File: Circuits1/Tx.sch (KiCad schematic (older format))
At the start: 28 parts, among them CON1 USB-MINI-B, SW1 SW_PUSH, U1 ATMEGA32U4, U2 LD1117, X1 QUARTZ

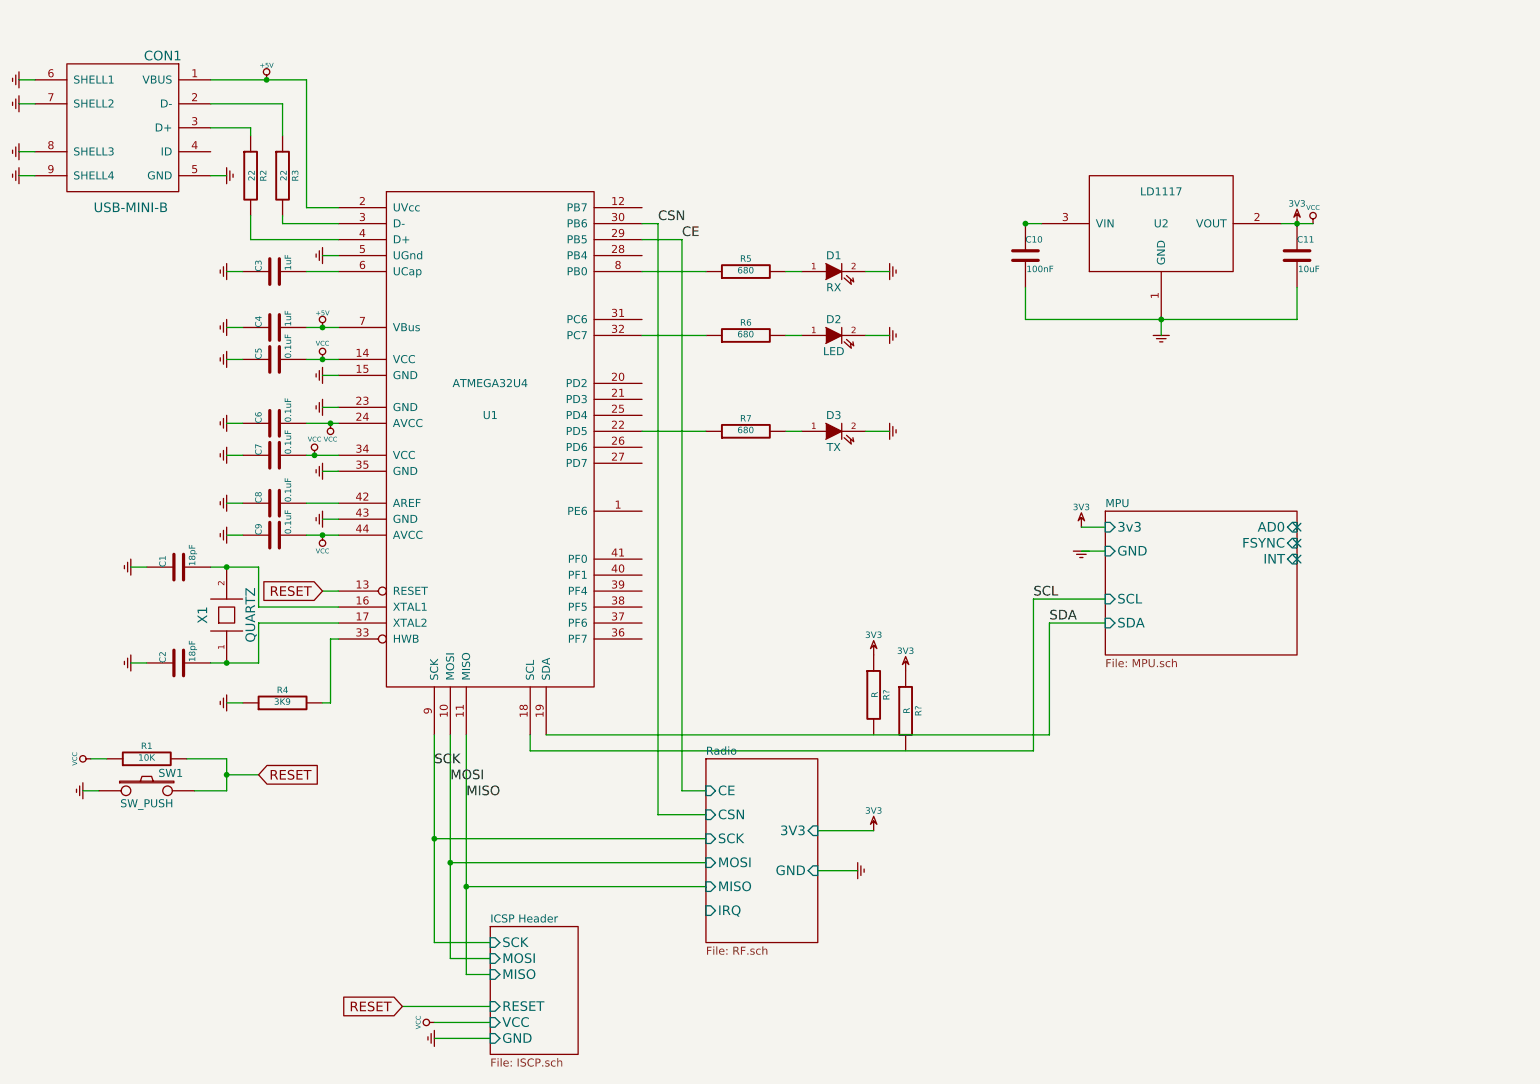
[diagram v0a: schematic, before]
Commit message: Tx Ground Planes
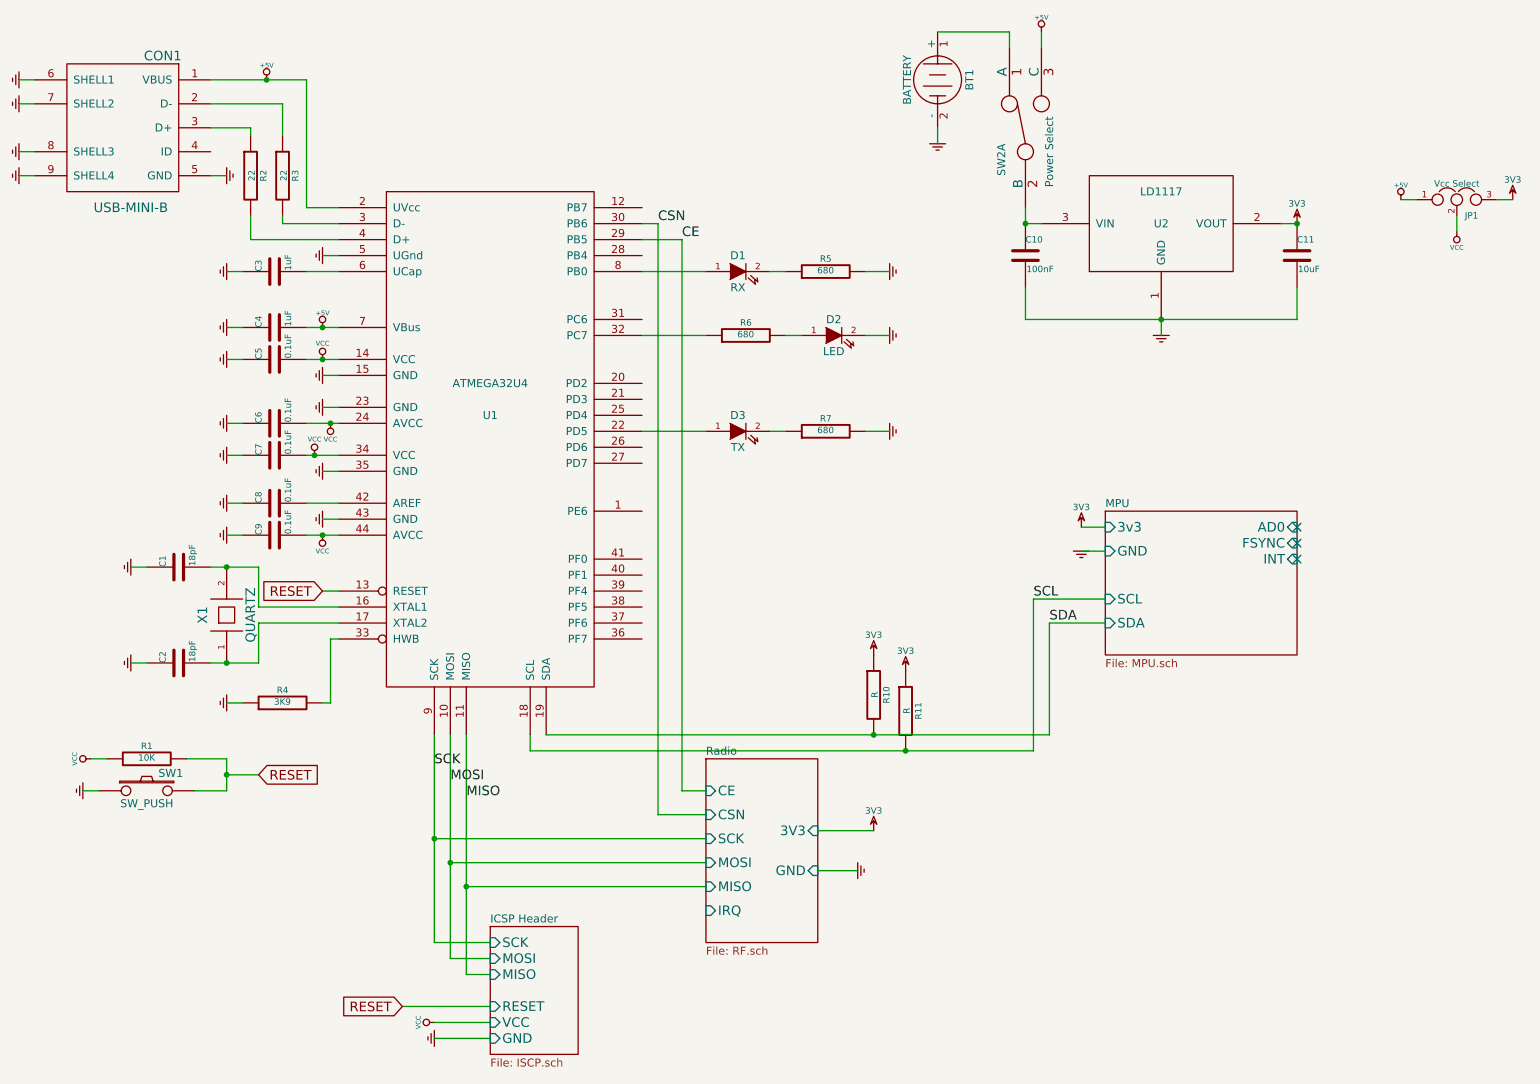
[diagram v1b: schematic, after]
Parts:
- added BT1: BATTERY, ~, symbol BATTERY
- added JP1: Vcc Select, ~, symbol JUMPER3
- added SW2: Power Select, ~, symbol DUAL_SWITCH_INV
- gave numbers to parts that had none: 2
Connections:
- net +5V: now also JP1.1, SW2.3 (C)
- net 3V3: now also JP1.3; no longer C5.2, C6.2, C7.2, C9.2, R1.1, U1.14 (VCC), U1.24 (AVCC), U1.34 (VCC), U1.44 (AVCC)
- net GND: now also R5.2, R7.2, BT1.2 (-); no longer D1.2 (K), D3.2 (K)
- net SCL: now also R11.2
- net SDA: now also R10.2
- net at U1.22 (PD5): now also D3.1 (A); no longer R7.1
- net at U1.8 (PB0): now also D1.1 (A); no longer R5.1
- net at C10.1, U2.3 (VIN): now also SW2.2 (B)
- new net: D1.2 (K), R5.1
- new net: D3.2 (K), R7.1
- new net: BT1.1 (+), SW2.1 (A)
- new net VCC: C5.2, C6.2, C7.2, C9.2, JP1.2, R1.1, U1.14 (VCC), U1.24 (AVCC), U1.34 (VCC), U1.44 (AVCC)
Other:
- moved on the sheet: D1, D3, R5, R7

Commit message: Neatened Schematics and Final PCB
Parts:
- added Hole1, Hole2: CONN_1, symbol CONN_1
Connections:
- net CE renamed Radio/CE
- net CSN renamed Radio/CSN
- no-connect marks 3 -> 21
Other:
- moved on the sheet: BT1, C1, C10, C11, C2, C3, C4, C5, C6, C7, C8, C9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

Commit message: Neatened up for report
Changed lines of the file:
@@
-EESchema Schematic File Version 2
+EESchema Schematic File Version 2  date Monday, 31 March 2014 17:10:11
 LIBS:power
 LIBS:device
@@
 Sheet 1 4
 Title ""
-Date "7 mar 2014"
+Date "31 mar 2014"
 Rev ""
 Comp ""
@@
 RESET
 $Sheet
-S 8000 1350 700  1150
+S 8400 1350 700  1150
 U 52AF81F8
 F0 "Radio" 50
 F1 "RF.sch" 50
-F2 "CE" I L 8000 1700 60
-F3 "CSN" I L 8000 1550 60
-F4 "SCK" I L 8000 1850 60
-F5 "MOSI" I L 8000 2000 60
-F6 "MISO" I L 8000 2150 60
-F7 "IRQ" I L 8000 2300 60
-F8 "GND" I R 8700 2050 60
-F9 "3V3" I R 8700 1800 60
+F2 "CE" I L 8400 1700 60
+F3 "CSN" I L 8400 1550 60
+F4 "SCK" I L 8400 1850 60
+F5 "MOSI" I L 8400 2000 60
+F6 "MISO" I L 8400 2150 60
+F7 "IRQ" I L 8400 2300 60
+F8 "GND" I R 9100 2050 60
+F9 "3V3" I R 9100 1800 60
 $EndSheet
 Wire Wire Line
@@
 L GND #PWR027
 U 1 1 52AFA1BE
-P 8950 2050
-F 0 "#PWR027" H 8950 2050 30  0001 C CNN
-F 1 "GND" H 8950 1980 30  0001 C CNN
-F 2 "" H 8950 2050 60  0000 C CNN
-F 3 "" H 8950 2050 60  0000 C CNN
-	1    8950 2050
-	0    -1   -1   0
-$EndComp
-Wire Wire Line
-	8700 2050 8950 2050
+P 9350 2050
+F 0 "#PWR027" H 9350 2050 30  0001 C CNN
+F 1 "GND" H 9350 1980 30  0001 C CNN
+F 2 "" H 9350 2050 60  0000 C CNN
+F 3 "" H 9350 2050 60  0000 C CNN
+	1    9350 2050
+	0    -1   -1   0
+$EndComp
+Wire Wire Line
+	9100 2050 9350 2050
 $Comp
 L LD1117 U2
@@
 L 3V3 #PWR030
 U 1 1 52B043A8
-P 9050 1800
-F 0 "#PWR030" H 9050 1900 40  0001 C CNN
-F 1 "3V3" H 9050 1925 40  0000 C CNN
-F 2 "" H 9050 1800 60  0000 C CNN
-F 3 "" H 9050 1800 60  0000 C CNN
-	1    9050 1800
-	1    0    0    -1
-$EndComp
-Wire Wire Line
-	9050 1800 8700 1800
+P 9450 1800
+F 0 "#PWR030" H 9450 1900 40  0001 C CNN
+F 1 "3V3" H 9450 1925 40  0000 C CNN
+F 2 "" H 9450 1800 60  0000 C CNN
+F 3 "" H 9450 1800 60  0000 C CNN
+	1    9450 1800
+	1    0    0    -1
+$EndComp
+Wire Wire Line
+	9450 1800 9100 1800
 $Sheet
 S 4950 6000 550  800
@@
 Wire Wire Line
 	3050 3750 3050 4000
-NoConn ~ 8000 2300
+NoConn ~ 8400 2300
 NoConn ~ 5900 4200
 NoConn ~ 5900 4100
@@
 	4800 5750 4450 5750
 Wire Wire Line
-	5900 1700 8000 1700
-Wire Wire Line
-	8000 1550 6850 1550
+	5900 1700 8400 1700
+Wire Wire Line
+	6850 1550 8400 1550
 Wire Wire Line
 	6850 1550 6850 1600
@@
 	6850 1600 5900 1600
 NoConn ~ 2750 1850
+Wire Wire Line
+	8400 1850 8100 1850
+Wire Wire Line
+	8400 2000 8100 2000
+Wire Wire Line
+	8400 2150 8100 2150
+Text GLabel 8100 1850 0    60   Input ~ 0
+SCK
+Text GLabel 8100 2000 0    60   Input ~ 0
+MOSI
+Text GLabel 8100 2150 0    60   Input ~ 0
+MISO
 $EndSCHEMATC
